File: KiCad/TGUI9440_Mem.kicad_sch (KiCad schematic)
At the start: 31 parts, among them J3 VGA, U10 HY514260B_SOJ40, U11 27C256, U41 74F541, U7 HY514260B_SOJ40, U8 HY514260B_SOJ40, U9 HY514260B_SOJ40

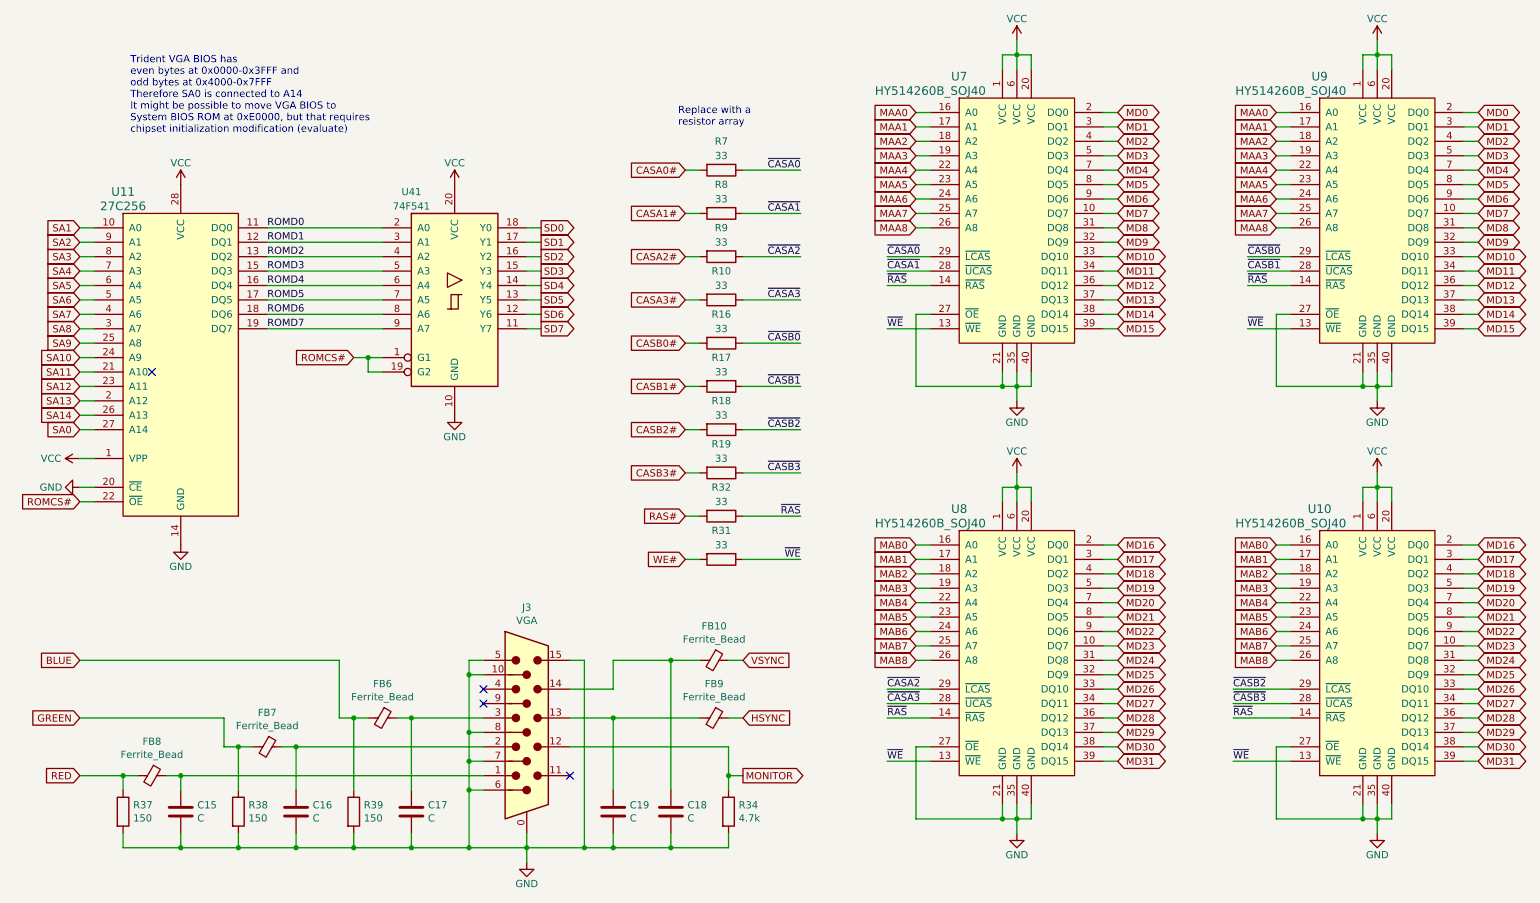
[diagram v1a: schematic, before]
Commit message: Version 0.4: Update chipset connection
Signed-off-by: Sergey Kiselev <skiselev@gmail.com>
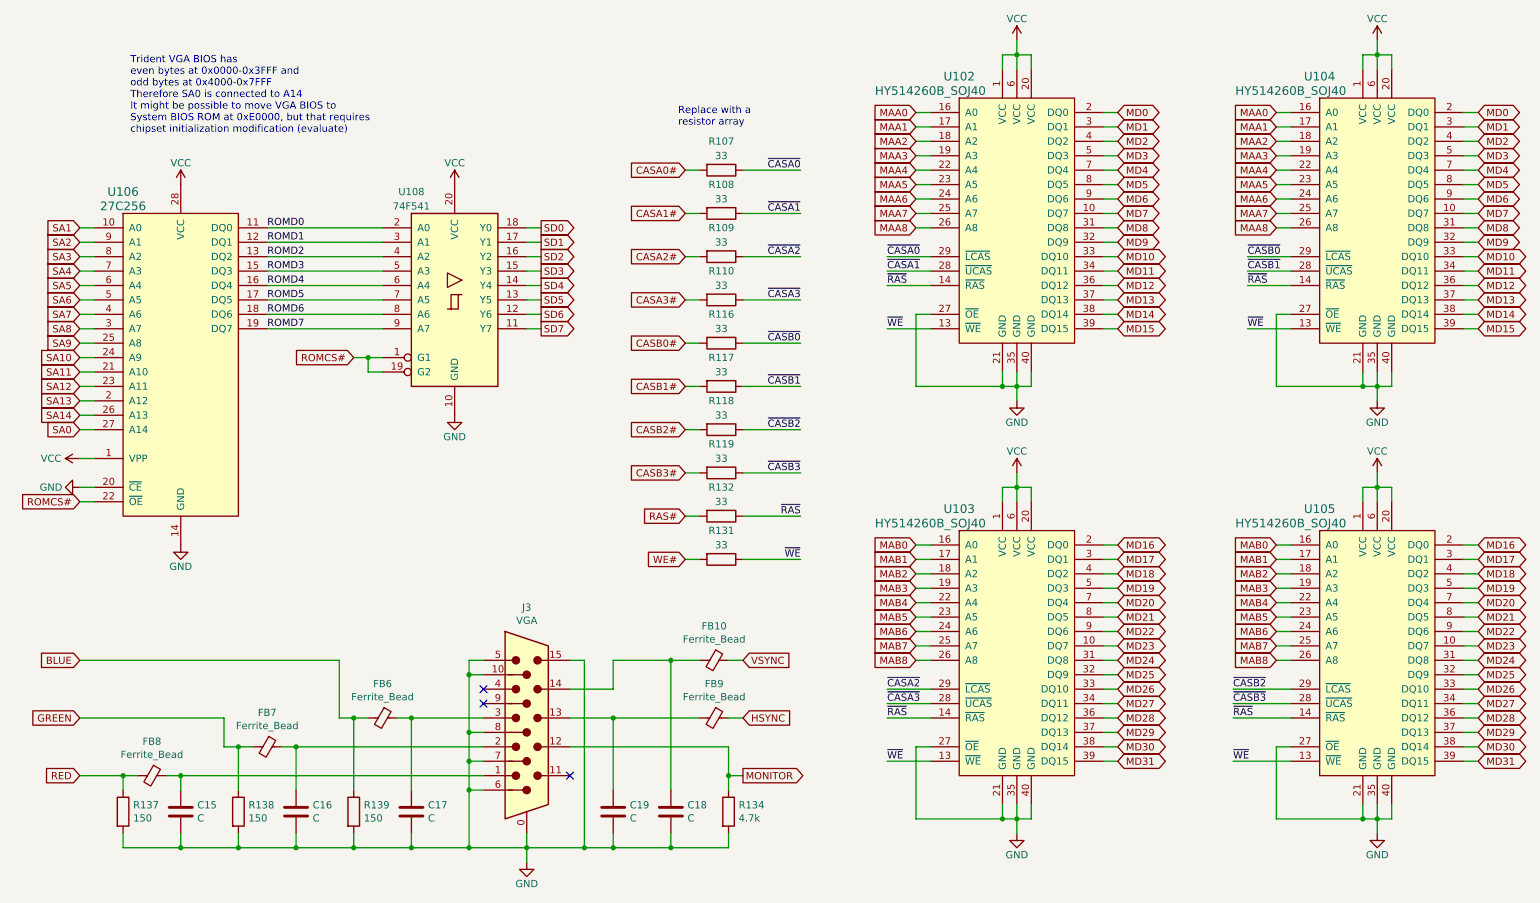
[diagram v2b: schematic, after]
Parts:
- C15, C16, C17, C18, C19: footprint (none) -> Capacitor_SMD:C_0603_1608Metric_Pad1.08x0.95mm_HandSolder
- FB10, FB6, FB7, FB8, FB9: footprint (none) -> Inductor_SMD:L_0603_1608Metric_Pad1.05x0.95mm_HandSolder; symbol Device:Ferrite_Bead_Small -> Device:FerriteBead_Small
- J3: footprint (none) -> My_Components:Conn_Dsub_DE15F
- R107: renamed from R7; footprint (none) -> Resistor_SMD:R_0612_1632Metric_Pad1.18x3.40mm_HandSolder
- R108: renamed from R8; footprint (none) -> Resistor_SMD:R_0612_1632Metric_Pad1.18x3.40mm_HandSolder
- R109: renamed from R9; footprint (none) -> Resistor_SMD:R_0612_1632Metric_Pad1.18x3.40mm_HandSolder
- R110: renamed from R10; footprint (none) -> Resistor_SMD:R_0612_1632Metric_Pad1.18x3.40mm_HandSolder
- R116: renamed from R16; footprint (none) -> Resistor_SMD:R_0612_1632Metric_Pad1.18x3.40mm_HandSolder
- R117: renamed from R17; footprint (none) -> Resistor_SMD:R_0612_1632Metric_Pad1.18x3.40mm_HandSolder
- R118: renamed from R18; footprint (none) -> Resistor_SMD:R_0612_1632Metric_Pad1.18x3.40mm_HandSolder
- R119: renamed from R19; footprint (none) -> Resistor_SMD:R_0612_1632Metric_Pad1.18x3.40mm_HandSolder
- R131: renamed from R31; footprint (none) -> Resistor_SMD:R_0612_1632Metric_Pad1.18x3.40mm_HandSolder
- R132: renamed from R32; footprint (none) -> Resistor_SMD:R_0612_1632Metric_Pad1.18x3.40mm_HandSolder
- R134: renamed from R34; footprint (none) -> Resistor_SMD:R_0612_1632Metric_Pad1.18x3.40mm_HandSolder
- R137: renamed from R37; footprint (none) -> Resistor_SMD:R_0612_1632Metric_Pad1.18x3.40mm_HandSolder
- R138: renamed from R38; footprint (none) -> Resistor_SMD:R_0612_1632Metric_Pad1.18x3.40mm_HandSolder
- R139: renamed from R39; footprint (none) -> Resistor_SMD:R_0612_1632Metric_Pad1.18x3.40mm_HandSolder
- U102: renamed from U7; footprint (none) -> Package_SO:SOJ-36_10.16x23.49mm_P1.27mm
- U103: renamed from U8; footprint (none) -> Package_SO:SOJ-36_10.16x23.49mm_P1.27mm
- U104: renamed from U9; footprint (none) -> Package_SO:SOJ-36_10.16x23.49mm_P1.27mm
- U105: renamed from U10; footprint (none) -> Package_SO:SOJ-36_10.16x23.49mm_P1.27mm
- U106: renamed from U11; footprint (none) -> My_Components:IC_DIP28_600
- U108: renamed from U41; footprint (none) -> My_Components:IC_DIP20_300
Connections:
- no-connect marks 4 -> 3

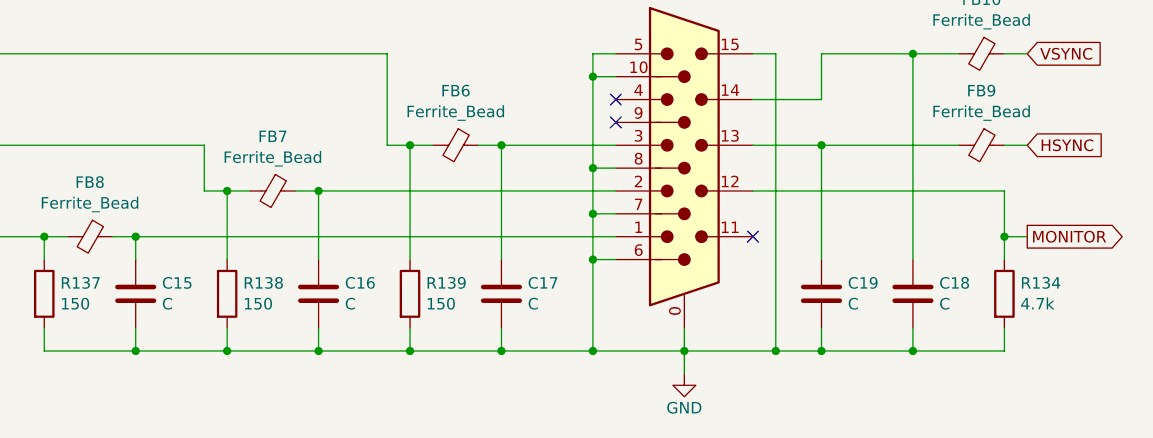
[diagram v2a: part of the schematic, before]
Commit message: More schematic updates. Remove old KiCad files
Signed-off-by: Sergey Kiselev <skiselev@gmail.com>
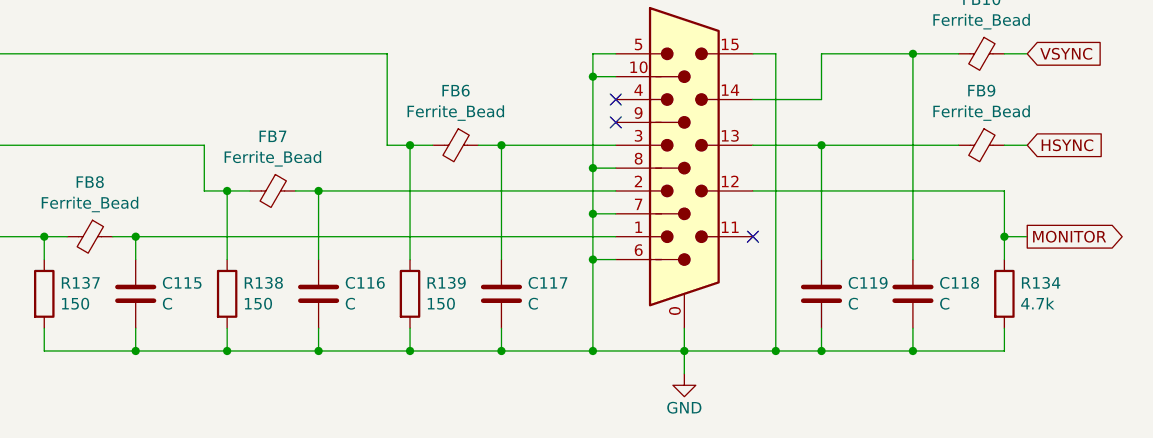
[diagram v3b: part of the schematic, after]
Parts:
- renumbered C15 to C115, C16 to C116, C17 to C117, C18 to C118, C19 to C119
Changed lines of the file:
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@@
   (symbol (lib_id "Device:C") (at 119.38 153.67 0) (unit 1)
     (in_bom yes) (on_board yes)
-    (property "Reference" "C19" (id 0) (at 122.301 152.5016 0)
+    (property "Reference" "C119" (id 0) (at 122.301 152.5016 0)
       (effects (font (size 1.27 1.27)) (justify left))
     )
@@
   (symbol (lib_id "Device:C") (at 129.54 153.67 0) (unit 1)
     (in_bom yes) (on_board yes)
-    (property "Reference" "C18" (id 0) (at 132.461 152.5016 0)
+    (property "Reference" "C118" (id 0) (at 132.461 152.5016 0)
       (effects (font (size 1.27 1.27)) (justify left))
     )
@@
   (symbol (lib_id "Device:C") (at 63.5 153.67 0) (unit 1)
     (in_bom yes) (on_board yes)
-    (property "Reference" "C16" (id 0) (at 66.421 152.5016 0)
+    (property "Reference" "C116" (id 0) (at 66.421 152.5016 0)
       (effects (font (size 1.27 1.27)) (justify left))
     )
@@
   (symbol (lib_id "Device:C") (at 83.82 153.67 0) (unit 1)
     (in_bom yes) (on_board yes)
-    (property "Reference" "C17" (id 0) (at 86.741 152.5016 0)
+    (property "Reference" "C117" (id 0) (at 86.741 152.5016 0)
       (effects (font (size 1.27 1.27)) (justify left))
     )
@@
   (symbol (lib_id "Device:C") (at 43.18 153.67 0) (unit 1)
     (in_bom yes) (on_board yes)
-    (property "Reference" "C15" (id 0) (at 46.101 152.5016 0)
+    (property "Reference" "C115" (id 0) (at 46.101 152.5016 0)
       (effects (font (size 1.27 1.27)) (justify left))
     )
